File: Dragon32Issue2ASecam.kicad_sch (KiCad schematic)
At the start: 1 part

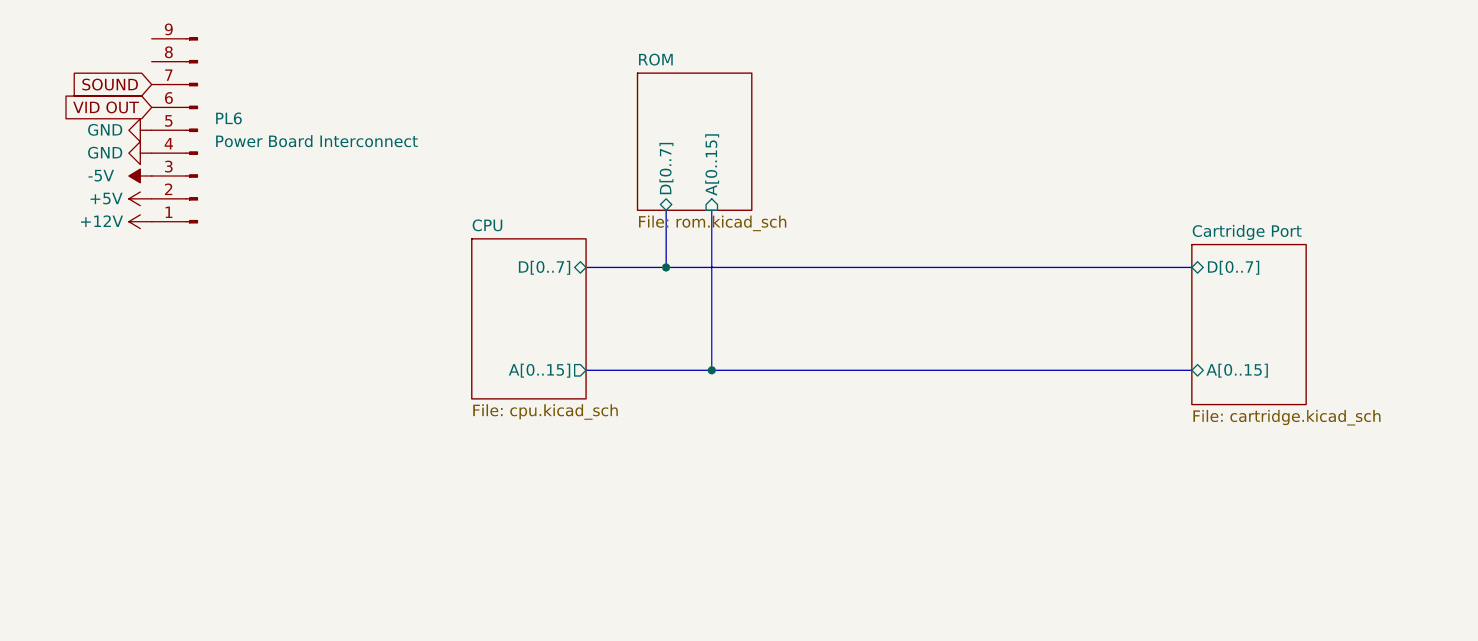
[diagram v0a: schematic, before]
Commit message: add sam and ram
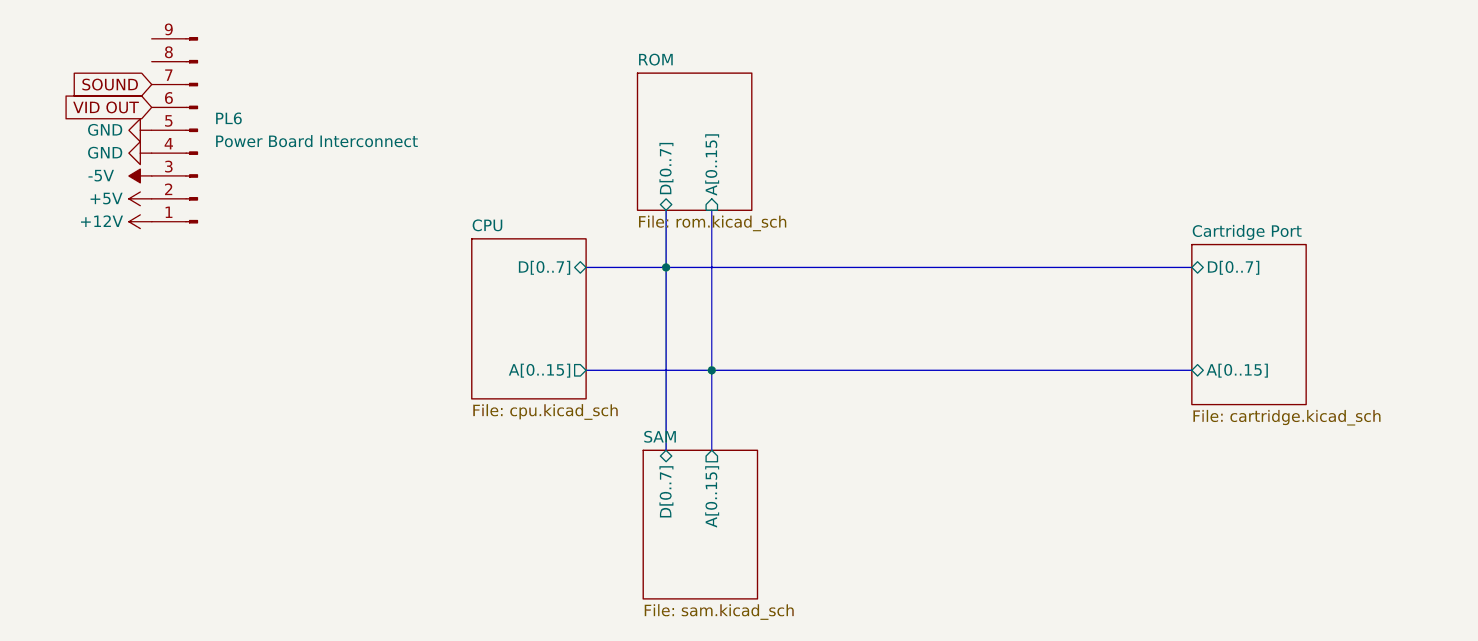
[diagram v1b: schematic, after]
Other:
- added sheet SAM (sam.kicad_sch)
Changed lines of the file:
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@@
+	(bus
+		(pts
+			(xy 95.25 59.69) (xy 95.25 68.58)
+		)
+		(stroke
+			(width 0)
+			(type default)
+		)
+	)
 	(bus
 		(pts
@@
 	(bus
 		(pts
-			(xy 90.17 48.26) (xy 148.59 48.26)
+			(xy 90.17 48.26) (xy 90.17 68.58)
 		)
 		(stroke
@@
 		(pts
 			(xy 81.28 48.26) (xy 90.17 48.26)
+		)
+		(stroke
+			(width 0)
+			(type default)
+		)
+	)
+	(bus
+		(pts
+			(xy 90.17 48.26) (xy 148.59 48.26)
 		)
 		(stroke
@@
 				)
 			)
+		)
+	)
+	(sheet
+		(at 87.63 68.58)
+		(size 12.7 16.51)
+		(fields_autoplaced yes)
+		(stroke
+			(width 0.1524)
+			(type solid)
+		)
+		(fill
+			(color 0 0 0 0.0000)
+		)
+		(property "Sheetname" "SAM"
+			(at 87.63 67.8684 0)
+			(effects
+				(font
+					(size 1.27 1.27)
+				)
+				(justify left bottom)
+			)
+		)
+		(property "Sheetfile" "sam.kicad_sch"
+			(at 87.63 85.6746 0)
+			(effects
+				(font
+					(size 1.27 1.27)
+				)
+				(justify left top)
+			)
+		)
+		(pin "A[0..15]" output
+			(at 95.25 68.58 90)
+			(effects
+				(font
+					(size 1.27 1.27)
+				)
+				(justify right)
+			)
+		)
+		(pin "D[0..7]" bidirectional
+			(at 90.17 68.58 90)
+			(effects
+				(font
+					(size 1.27 1.27)
+				)
+				(justify right)
+			)
+		)
+		(instances
+			(project "Dragon32Issue2ASecam"
+				(path "/e3d9e4a2-26cb-4482-98c1-138d9a22d1eb"
+					(page "5")
+				)
+			)

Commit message: add PIA and VDG to schematics
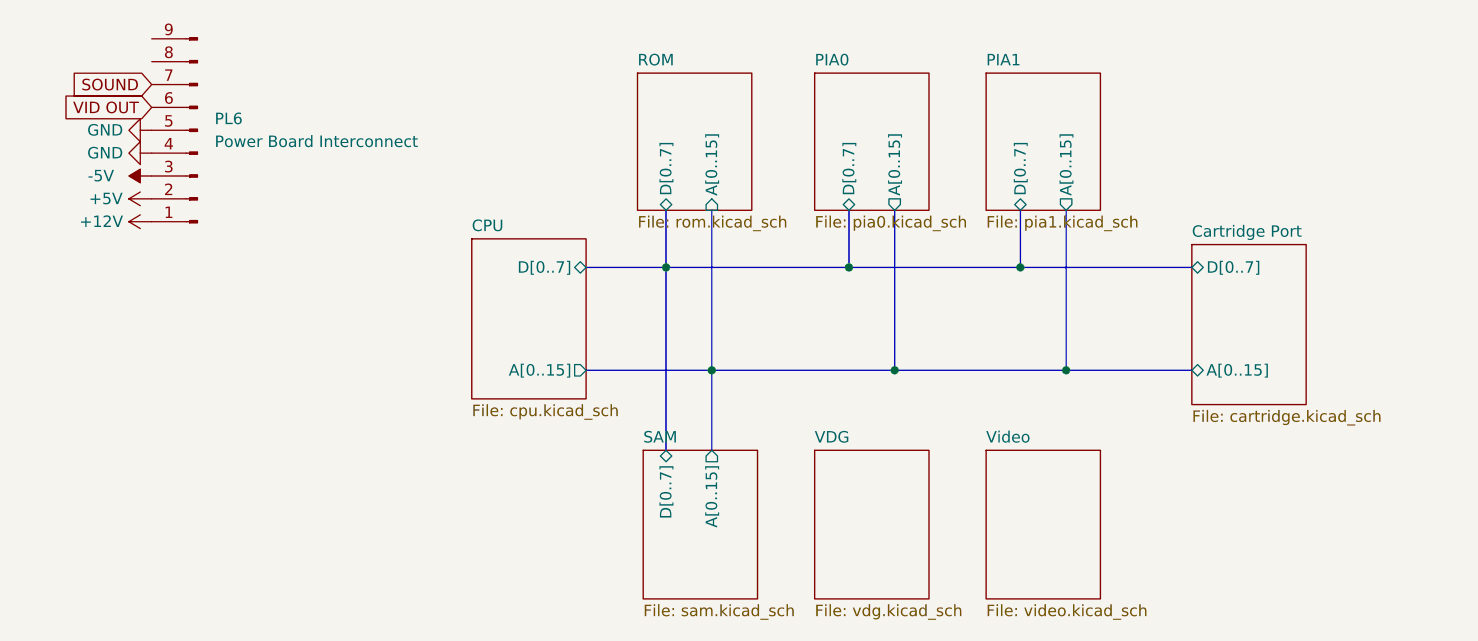
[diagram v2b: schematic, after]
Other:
- added sheet PIA0 (pia0.kicad_sch)
- added sheet PIA1 (pia1.kicad_sch)
- added sheet VDG (vdg.kicad_sch)
- added sheet Video (video.kicad_sch)

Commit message: video circuit tracing
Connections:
- net GND: no longer PL6.5 (Pin_5)
- new net GNDA: PL6.5 (Pin_5)
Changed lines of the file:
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@@
 	)
 	(symbol
-		(lib_id "power:GND")
+		(lib_id "power:GNDA")
 		(at 33.02 33.02 270)
 		(unit 1)
@@
 			)
 		)
-		(property "Value" "GND"
-			(at 29.845 33.0199 90)
+		(property "Value" "GNDA"
+			(at 29.21 33.0199 90)
 			(effects
 				(font
@@
 			)
 		)
-		(property "Description" ""
+		(property "Description" "Power symbol creates a global label with name \"GNDA\" , analog ground"
 			(at 33.02 33.02 0)
 			(effects
@@
 		)
 		(instances
-			(project "Dragon32Issue2ASecam"
+			(project ""
 				(path "/e3d9e4a2-26cb-4482-98c1-138d9a22d1eb"
 					(reference "#PWR020")

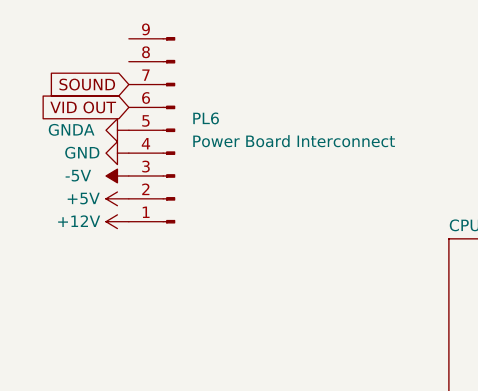
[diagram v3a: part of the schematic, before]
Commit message: FM generator routing
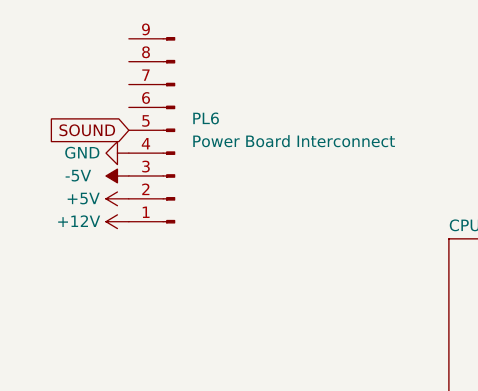
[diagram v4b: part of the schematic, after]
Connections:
- net GNDA is gone; now on net SOUND: PL6.5 (Pin_5)
- net SOUND: no longer PL6.7 (Pin_7)
- net VID OUT: no longer names the net of PL6.6 (Pin_6)
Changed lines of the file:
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@@
 	(global_label "SOUND"
 		(shape input)
-		(at 33.02 27.94 180)
+		(at 33.02 33.02 180)
 		(fields_autoplaced yes)
 		(effects
@@
 		)
 		(property "Intersheetrefs" "${INTERSHEET_REFS}"
-			(at 24.2974 27.94 0)
-			(effects
-				(font
-					(size 1.27 1.27)
-				)
-				(justify right)
-				(hide yes)
-			)
-		)
-	)
-	(global_label "VID OUT"
-		(shape input)
-		(at 33.02 30.48 180)
-		(fields_autoplaced yes)
-		(effects
-			(font
-				(size 1.27 1.27)
-			)
-			(justify right)
-		)
-		(property "Intersheetrefs" "${INTERSHEET_REFS}"
-			(at 23.4144 30.48 0)
+			(at 24.2974 33.02 0)
 			(effects
 				(font
@@
 					(unit 1)
 				)
-			)
-		)
-	)
-	(symbol
-		(lib_id "power:GNDA")
-		(at 33.02 33.02 270)
-		(unit 1)
-		(exclude_from_sim no)
-		(in_bom yes)
-		(on_board yes)
-		(dnp no)
-		(fields_autoplaced yes)
-		(property "Reference" "#PWR020"
-			(at 26.67 33.02 0)
-			(effects
-				(font
-					(size 1.27 1.27)
-				)
-				(hide yes)
-			)
-		)
-		(property "Value" "GNDA"
-			(at 29.21 33.0199 90)
-			(effects
-				(font
-					(size 1.27 1.27)
-				)
-				(justify right)
-			)
-		)
-		(property "Footprint" ""
-			(at 33.02 33.02 0)
-			(effects
-				(font
-					(size 1.27 1.27)
-				)
-				(hide yes)
-			)
-		)
-		(property "Datasheet" ""
-			(at 33.02 33.02 0)
-			(effects
-				(font
-					(size 1.27 1.27)
-				)
-				(hide yes)
-			)
-		)
-		(property "Description" "Power symbol creates a global label with name \"GNDA\" , analog ground"
-			(at 33.02 33.02 0)
-			(effects
-				(font
-					(size 1.27 1.27)
-				)
-				(hide yes)
-			)
-		)
-		(pin "1"
-		)
-		(instances
-			(project ""
-				(path "/e3d9e4a2-26cb-4482-98c1-138d9a22d1eb"
-					(reference "#PWR020")
-					(unit 1)
-				)

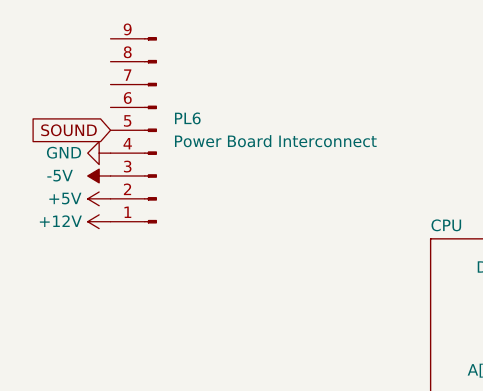
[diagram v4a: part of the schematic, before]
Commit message: complete physical layout
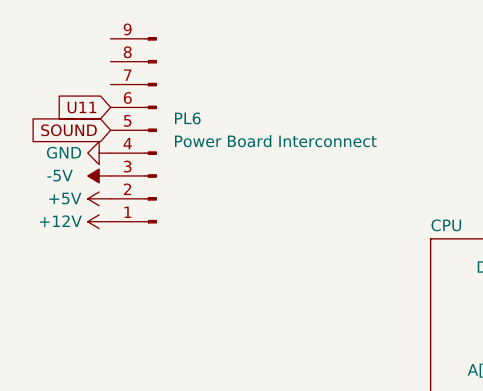
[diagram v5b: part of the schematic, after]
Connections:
- net U11: now reaches PL6.6 (Pin_6)
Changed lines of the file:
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@@
+		)
+	)
+	(global_label "U11"
+		(shape input)
+		(at 33.02 30.48 180)
+		(fields_autoplaced yes)
+		(effects
+			(font
+				(size 1.27 1.27)
+			)
+			(justify right)
+		)
+		(property "Intersheetrefs" "${INTERSHEET_REFS}"
+			(at 26.2853 30.48 0)
+			(effects
+				(font
+					(size 1.27 1.27)
+				)
+				(justify right)
+				(hide yes)
+			)
 		)
 	)

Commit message: fm circuit routing
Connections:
- net phiA: now reaches PL6.8 (Pin_8)
- net phiB: now reaches PL6.9 (Pin_9)
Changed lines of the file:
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@@
+		)
+	)
+	(global_label "phiB"
+		(shape input)
+		(at 33.02 22.86 180)
+		(fields_autoplaced yes)
+		(effects
+			(font
+				(size 1.27 1.27)
+			)
+			(justify right)
+		)
+		(property "Intersheetrefs" "${INTERSHEET_REFS}"
+			(at 25.862 22.86 0)
+			(effects
+				(font
+					(size 1.27 1.27)
+				)
+				(justify right)
+				(hide yes)
+			)
 		)
 	)
@@
 			(effects
 				(font
+					(size 1.27 1.27)
+				)
+				(justify right)
+				(hide yes)
+			)
+		)
+	)
+	(global_label "phiA"
+		(shape input)
+		(at 33.02 25.4 180)
+		(fields_autoplaced yes)
+		(effects
+			(font
+				(size 1.27 1.27)
+			)
+			(justify right)
+		)
+		(property "Intersheetrefs" "${INTERSHEET_REFS}"
+			(at 26.0434 25.4 0)
+			(effects
+				(font

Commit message: trace work complete
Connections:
- net LUMA'2: now reaches PL6.7 (Pin_7)
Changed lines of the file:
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@@
+		)
+	)
+	(global_label "LUMA'2"
+		(shape input)
+		(at 33.02 27.94 180)
+		(fields_autoplaced yes)
+		(effects
+			(font
+				(size 1.27 1.27)
+			)
+			(justify right)
+		)
+		(property "Intersheetrefs" "${INTERSHEET_REFS}"
+			(at 23.3219 27.94 0)
+			(effects
+				(font
+					(size 1.27 1.27)
+				)
+				(justify right)
+				(hide yes)
+			)
 		)
 	)

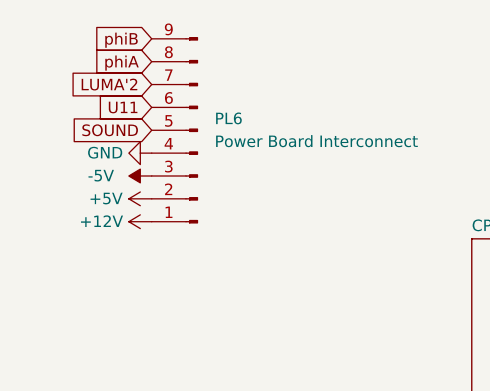
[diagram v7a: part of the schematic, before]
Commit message: resolve missing connections
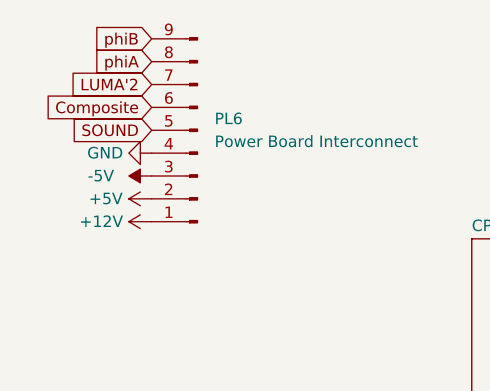
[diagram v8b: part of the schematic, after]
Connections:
- net U11 renamed Composite
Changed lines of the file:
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@@
 		)
 	)
-	(global_label "U11"
+	(global_label "Composite"
 		(shape input)
 		(at 33.02 30.48 180)
@@
 		)
 		(property "Intersheetrefs" "${INTERSHEET_REFS}"
-			(at 26.2853 30.48 0)
+			(at 20.1773 30.48 0)
 			(effects
 				(font
